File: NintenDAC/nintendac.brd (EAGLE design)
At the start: 42 x 42 mm, 36 parts, among them IC2 REG1117, U1 STM32F10XRXT6, X1 USB-MICROB

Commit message: board cleanup
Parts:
- removed C4: (no value), backplane:C1210
- removed IC2: REG1117, backplane:SOT223
- added D1, D2: (no value), nintendac_mini:SOD-123
- added U2: (no value), nintendac_mini:SOT23-5
- moved C2 1.25 mm to (22.3, 8.86)
- moved JP2 1.17 mm to (38.0, 25.8)
- moved S1 1.02 mm to (10.3, 38.5)
- moved U1 0.90 mm to (20.1, 25.8)
- moved Y1 0.90 mm to (20.1, 36.4)
- moved R8 0.90 mm to (12.1, 36.0)
- moved C11 0.90 mm to (30.0, 35.1)
- moved C12 0.90 mm to (30.0, 39.5)
- moved JP3 0.90 mm to (3.05, 25.8)
- moved Y2 0.90 mm to (27.2, 37.2)
- moved S2 0.90 mm to (23.0, 12.4)
- moved R6 0.90 mm to (30.1, 27.5)
- moved C7 0.90 mm to (12.6, 20.4)
- moved C5 0.90 mm to (26.7, 31.5)
- moved C6 0.90 mm to (25.5, 19.2)
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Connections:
- new net N$2: D1.C, D2.C, U2.1, U2.3
- net +3V3: now also U2.5; no longer IC2.2
- net GND: now also U2.2; no longer C4.2, IC2.1
- net N$58: now also D2.A, X1.VBUS
- net N$66: now also D1.A; no longer C4.1, IC2.3, X1.VBUS
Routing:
- net N$58: track 15.1 -> 62.4 mm, vias 0 -> 1
- net N$2: track 0.00 -> 12.9 mm
- net N$66: track 22.7 -> 19.2 mm
- net GND: track 49.1 -> 46.4 mm
- net N$24: track 21.1 -> 19.2 mm
- net N$22: track 28.0 -> 26.5 mm
- net N$21: track 25.3 -> 24.2 mm
- net N$3: track 21.2 -> 20.4 mm
- net N$19: track 18.3 -> 17.5 mm
- net N$17: track 11.6 -> 10.7 mm
- net N$4: track 21.3 -> 20.5 mm
- net N$18: track 12.0 -> 11.1 mm
- net N$16: track 13.1 -> 12.2 mm
- net N$1: track 36.2 -> 35.4 mm
- net LDAC: track 22.8 -> 22.1 mm
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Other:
- board size 42 x 42 mm -> 41 x 41 mm
- board text added: "G"

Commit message: board cleanup
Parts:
- moved S2 0.76 mm to (22.2, 12.4)
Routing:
- net N$30: track 28.8 -> 28.0 mm
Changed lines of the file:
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@@
 <attribute name="VALUE" x="3.175" y="3.429" size="0.4064" layer="27" rot="R90"/>
 </element>
-<element name="S2" library="Adafruit Feather M0 Adalogger" package="KMR2" value="SWITCH-MOMENTARY-2TURTLE" x="22.987" y="12.446"/>
+<element name="S2" library="Adafruit Feather M0 Adalogger" package="KMR2" value="SWITCH-MOMENTARY-2TURTLE" x="22.225" y="12.446"/>
 <element name="D1" library="nintendac_mini" package="SOD-123" value="" x="22.4282" y="5.6896" smashed="yes" rot="R180">
 <attribute name="NAME" x="19.2532" y="6.0706" size="0.8128" layer="25" ratio="18" rot="R180"/>
@@
 <wire x1="18.4912" y1="7.2136" x2="20.1422" y2="8.8646" width="0.3556" layer="1"/>
 <wire x1="20.1422" y1="8.8646" x2="20.8758" y2="8.8646" width="0.3556" layer="1"/>
-<via x="23.6982" y="12.4206" extent="1-16" drill="0.508"/>
-<wire x1="23.6982" y1="12.4206" x2="23.7236" y2="12.446" width="0.3556" layer="1"/>
-<wire x1="23.7236" y1="12.446" x2="25.387" y2="12.446" width="0.3556" layer="1"/>
 <wire x1="7.887" y1="38.481" x2="7.9886" y2="38.5826" width="0.254" layer="1"/>
 <wire x1="7.9886" y1="38.5826" x2="9.398" y2="38.5826" width="0.254" layer="1"/>
+<via x="22.8092" y="12.4206" extent="1-16" drill="0.508"/>
+<wire x1="22.8092" y1="12.4206" x2="24.625" y2="12.4206" width="0.254" layer="1"/>
+<wire x1="24.625" y1="12.4206" x2="24.625" y2="12.446" width="0.254" layer="1"/>
 </signal>
 <signal name="+3V3">
@@
 <wire x1="17.9832" y1="16.2306" x2="17.9832" y2="13.4366" width="0.254" layer="1"/>
 <wire x1="17.9832" y1="13.4366" x2="18.9738" y2="12.446" width="0.254" layer="1"/>
-<wire x1="18.9738" y1="12.446" x2="20.587" y2="12.446" width="0.254" layer="1"/>
+<wire x1="18.9738" y1="12.446" x2="19.825" y2="12.446" width="0.254" layer="1"/>
 </signal>
 <signal name="N$31">

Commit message: added EEPROM
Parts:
- added IC1: 24LC64ST, nintendac_mini:TSSOP8
- added R11, R12: (no value), SparkFun-Passives:0805
- added TP1: TEST-POINT3X5, SparkFun-Connectors:PAD.03X.05
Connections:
- new net N$67: IC1.6, R11.1, U1.29
- new net N$68: IC1.5, R12.1, U1.30
- new net N$69: TP1.P$1, U1.28
- net +3V3: now also IC1.8, R11.2, R12.2
- net GND: now also IC1.1, IC1.2, IC1.3, IC1.4, IC1.7
- net LDAC: no longer U1.28
- net N$20: no longer U1.30
- net N$21: no longer U1.29
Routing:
- net N$67: track 0.00 -> 29.6 mm, vias 0 -> 1
- net N$68: track 0.00 -> 23.3 mm, vias 0 -> 1
- net LDAC: track 22.1 -> 5.65 mm
- net N$21: track 24.2 -> 9.23 mm
- net N$20: track 22.5 -> 8.37 mm
- net N$69: track 0.00 -> 8.40 mm
- net +3V3: track 53.1 -> 60.1 mm, vias 0 -> 2
- net GND: track 46.6 -> 47.4 mm

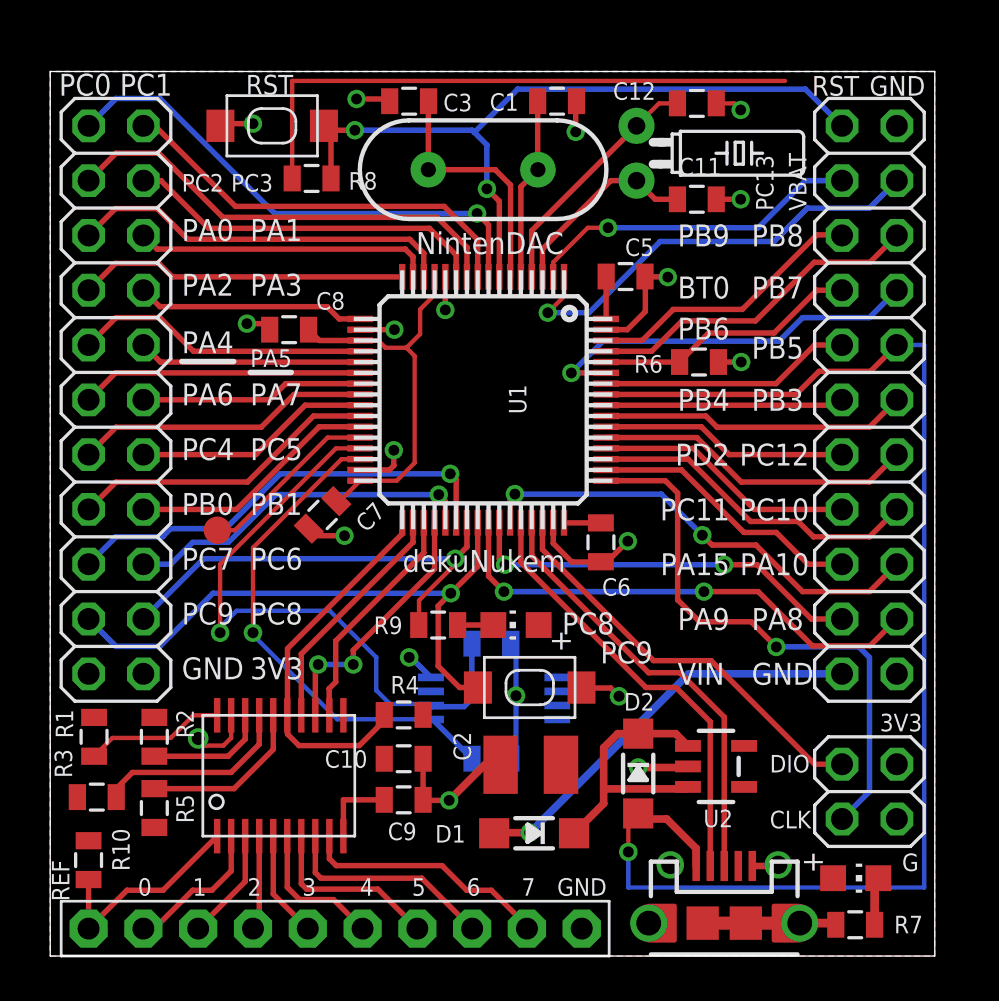
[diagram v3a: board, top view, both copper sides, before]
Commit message: removed wkup from headers
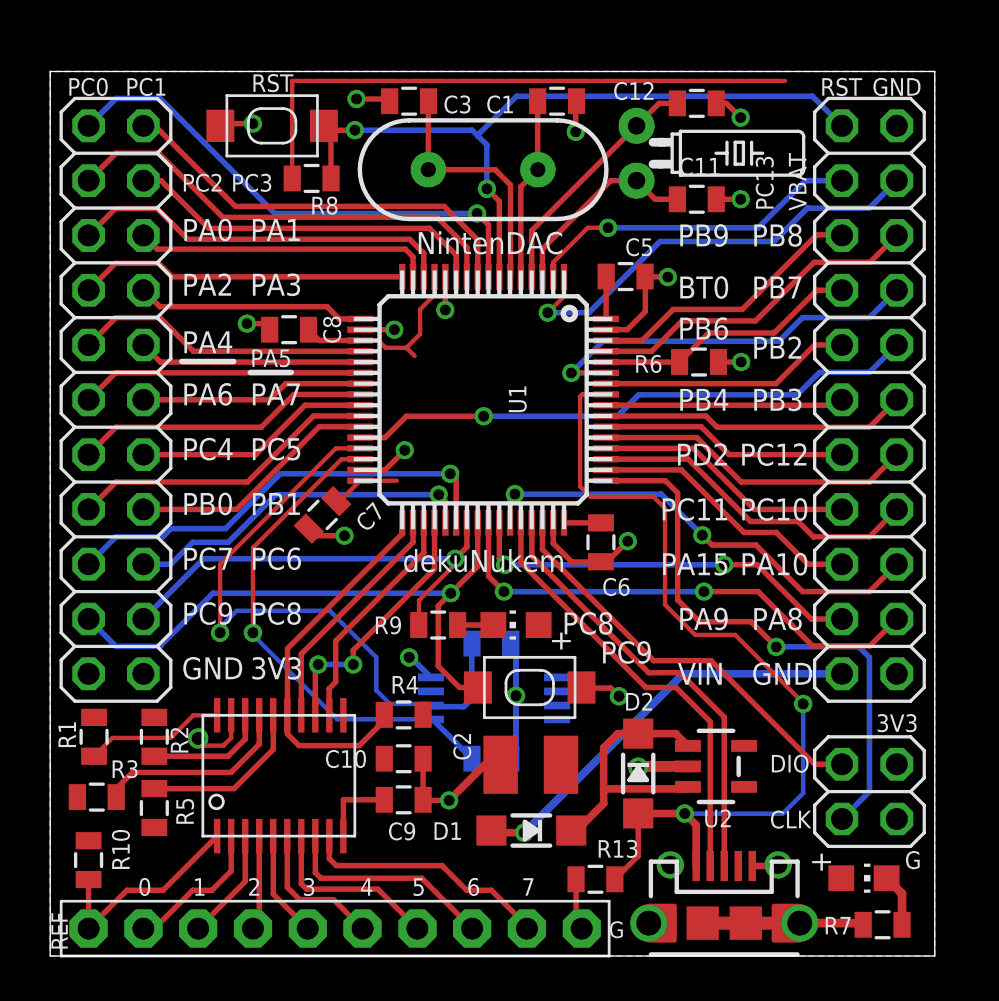
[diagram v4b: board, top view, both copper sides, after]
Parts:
- removed TP1: TEST-POINT3X5, SparkFun-Connectors:PAD.03X.05
- added R13: (no value), SparkFun-Passives:0805
- moved R7 1.27 mm to (38.6, 1.45)
- moved LED1 0.38 mm to (37.7, 3.61)
- moved D1 0.18 mm to (22.3, 5.82)
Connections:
- net GND: now also R13.1
- net N$58: now also R13.2; no longer JP2.13
- net N$69: now also JP2.13; no longer TP1.P$1
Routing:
- net N$58: track 62.4 -> 41.3 mm, vias 1 -> 2
- net N$69: track 8.40 -> 26.7 mm, vias 0 -> 1
- net +3V3: track 60.1 -> 53.9 mm
- net GND: track 47.4 -> 51.3 mm
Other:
- board text added: "PB2"
- board text removed: "PB5"
